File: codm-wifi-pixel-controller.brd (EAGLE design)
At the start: 59 x 25.5 mm, 48 parts, among them U1 AP62XXX-TSOT26, U2 REG710NA-5/250, U3 SN74AHCT125D, U4 ESP-WROOM-32

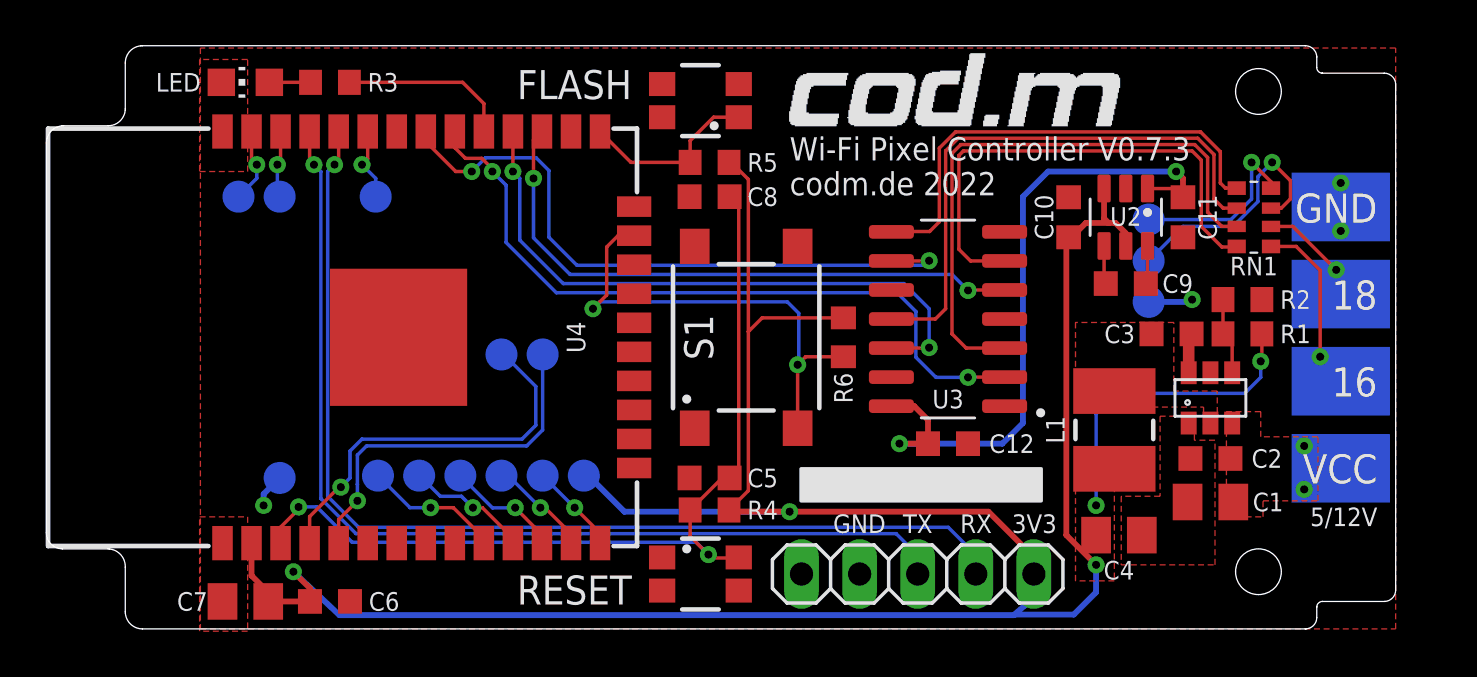
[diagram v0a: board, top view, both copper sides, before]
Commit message: added reverse polarity protection
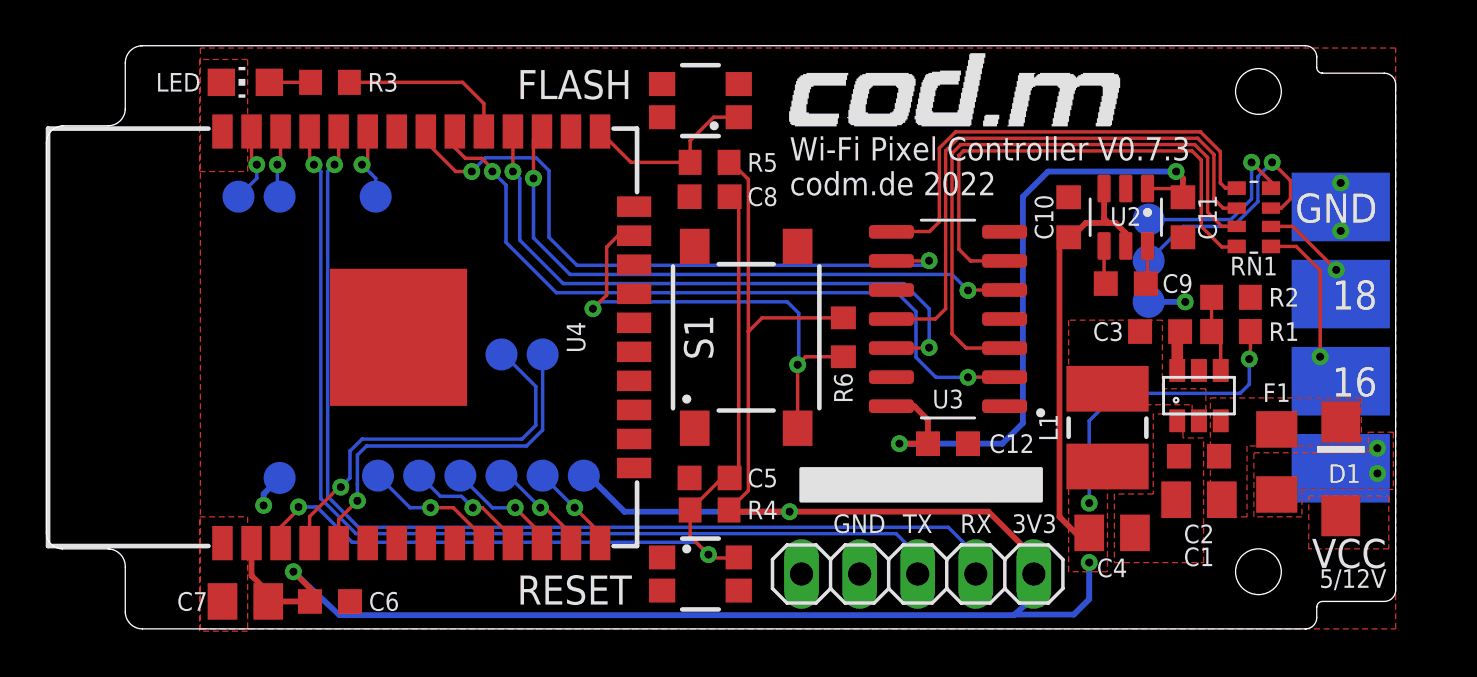
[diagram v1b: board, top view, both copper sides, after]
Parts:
- added D1: SK34A, diode:DO214AC
- added F1: 8V 500mA, adafruit:R1206
- moved C1 0.51 mm to (50.4, 5.65)
- moved C2 0.51 mm to (50.4, 7.55)
- moved C3 0.51 mm to (48.7, 13.0)
- moved R1 0.51 mm to (51.8, 13.0)
- moved R2 0.51 mm to (51.8, 14.5)
- moved U1 0.51 mm to (50.4, 10.2)
- moved L1 0.32 mm to (46.4, 8.80)
- moved C4 0.32 mm to (46.6, 4.20)
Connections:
- new net VCCF: C1.2, C2.1, D1.C, F1.2, U1.VIN
- net GND: now also D1.A
- net VCC: now also F1.1; no longer C1.2, C2.1, U1.VIN
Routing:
- net +3V3: track 124.5 -> 123.6 mm
- added copper zone on layer 1, net VCCF

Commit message: new version 0.7.4 with fixes
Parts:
- removed C8: 100n, rcl:C0603K
- added TP16: PTR1TP14R, testpad:TP14R
- JP1: device pinhead:1X05 -> codm:1X05
- U3: value SN74AHCT125D -> SN74AHCT125PWR; device SN74AHCT125D:SOIC127P600X175-14N -> SN74AHCT125PWR:SOP65P640X120-14N
- moved C11 23.8 mm to (28.1, 8.00)
- moved RN1 21.9 mm to (30.9, 18.6), turned to 180 degrees
- moved U2 19.0 mm to (31.0, 8.10), turned to 0 degrees
- moved C10 18.5 mm to (31.0, 5.60), turned to 0 degrees
- moved C9 15.0 mm to (33.9, 8.10), turned to 270 degrees
- moved S1 9.70 mm to (40.3, 12.8)
- moved C12 8.94 mm to (31.0, 11.1)
- moved TP7 8.70 mm to (48.2, 23.0)
- moved U3 8.48 mm to (31.0, 14.5)
- moved D1 7.86 mm to (49.0, 5.00)
- moved R6 7.74 mm to (40.3, 7.25), turned to 180 degrees
- moved C5 6.38 mm to (33.8, 2.40), turned to 270 degrees
- moved C4 5.00 mm to (46.6, 9.20)
- moved R4 4.33 mm to (32.3, 2.40), turned to 270 degrees
- moved L1 4.30 mm to (46.4, 13.1)
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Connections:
- net BTN: now also S1.1; no longer S1.2
- net GND: now also FLASH.4, RESET.2, S1.2, TP16.TP; no longer C8.1, FLASH.3, RESET.1, S1.1
- net RESET: no longer C8.2
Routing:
- net IO18-5VR: track 4.78 -> 29.9 mm
- net +5V: track 29.9 -> 8.36 mm, vias 2 -> 0
- net IO16-5VR: track 7.80 -> 28.2 mm
- net IO18-5V: track 25.9 -> 6.05 mm
- net IO17-5V: track 24.8 -> 5.19 mm
- net IO16-5V: track 22.0 -> 3.38 mm
- net IO19-5V: track 20.6 -> 2.62 mm
- net RESET: track 39.3 -> 26.8 mm
- net IO19-5VR: track 7.95 -> 20.1 mm
- net IO17: track 27.4 -> 16.7 mm
- net IO18: track 31.6 -> 22.0 mm
- net IO19: track 28.6 -> 19.3 mm
- net IO17-5VR: track 10.8 -> 19.3 mm
- net IO16: track 26.4 -> 18.6 mm
- net +3V3: track 123.6 -> 116.5 mm, vias 5 -> 7
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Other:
- board text added: "90060-0.7.4"
- board text added: "Wi-Fi Pixel Controller V0.7.4"
- board text added: "Wi-Fi Pixel Controller V0.7.4 codm.de 2022"
- board text added: "codm.de 2022"
- board text removed: "90060-0.7.3"
- board text removed: "Wi-Fi Pixel Controller V0.7.3 codm.de 2022"
- board text removed: "Wi-Fi Pixel Controller V0.7.3 codm.de, 2022 CC-BY-NC-SA"

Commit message: finetuning 0.7.4
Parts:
- removed R5: 10k, rcl:R0603
- added U$2: (no value), codm:WLED-INSIDE-LOGO-10MM
- F1: value 8V 500mA -> 24V 500mA
- moved U$102 9.31 mm to (36.5, 11.2)
- moved U$100 4.53 mm to (31.9, 6.60)
- moved R6 0.10 mm to (40.2, 7.25)
- moved S1 0.10 mm to (40.2, 12.8)
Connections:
- net +3V3: no longer R5.1
- net GPIO0: no longer R5.2
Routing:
- net +3V3: track 116.5 -> 97.4 mm, vias 7 -> 5
- net GPIO0: track 9.36 -> 6.92 mm
- net +5V: track 8.36 -> 6.84 mm
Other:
- board text added: "IO0"
- board text added: "IO15"

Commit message: after prototype 0.7.4 - final 0.8
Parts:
- removed C12: 100n, rcl:C0603K
- added C8: 2.2uF, rcl:C0603K
- C11: value 2.2uF -> 100n
- moved C11 4.24 mm to (31.0, 11.1), turned to 180 degrees
- moved C9 3.83 mm to (31.0, 5.60), turned to 0 degrees
- moved C10 3.76 mm to (28.1, 8.00), turned to 90 degrees
- renumbered R6 to R5
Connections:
- net +3V3: now also C9.2; no longer C10.2
- net +5V: now also C10.2; no longer C12.2
- net GND: now also C9.1; no longer C12.1
- net N$5: now also C8.1; no longer C9.1
- net N$8: now also C8.2; no longer C9.2
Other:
- board text added: "90060-0.8"
- board text added: "CC-BY-NC-SA 4.0"
- board text added: "Wi-Fi Pixel Controller V0.8"
- board text added: "Wi-Fi Pixel Controller V0.8 codm.de 2022"
- board text removed: "90060-0.7.4"
- board text removed: "Wi-Fi Pixel Controller V0.7.4"
- board text removed: "Wi-Fi Pixel Controller V0.7.4 codm.de 2022"
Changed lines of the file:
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@@
 <text x="43.95" y="3.7" size="0.8128" layer="25" font="vector" align="center">RX</text>
 <text x="46.5" y="3.7" size="0.8128" layer="25" font="vector" align="center">3V3</text>
-<text x="34.6" y="21.1" size="1.016" layer="25" font="vector" ratio="12" align="top-left">Wi-Fi Pixel Controller V0.7.4
+<text x="34.6" y="21.1" size="1.016" layer="25" font="vector" ratio="12" align="top-left">Wi-Fi Pixel Controller V0.8
 codm.de 2022</text>
-<text x="2.4" y="13.2" size="1.4224" layer="26" font="vector" rot="MR90" align="center">90060-0.7.4</text>
-<text x="58.2" y="18.4" size="1.27" layer="25" ratio="15" align="center-right">GND</text>
-<text x="58.2" y="14.6" size="1.27" layer="25" ratio="15" align="center-right">18</text>
-<text x="58.2" y="10.8" size="1.27" layer="25" ratio="15" align="center-right">16</text>
-<text x="58.2" y="7" size="1.27" layer="25" ratio="15" align="center-right">VCC</text>
-<text x="29.5" y="17.1" size="1.4224" layer="26" ratio="12" rot="MR0" align="center">Wi-Fi Pixel Controller V0.7.4</text>
+<text x="2.4" y="13.2" size="1.4224" layer="26" font="vector" rot="MR90" align="center">90060-0.8</text>
+<text x="58.2" y="18.4" size="1.27" layer="25" ratio="20" align="center-right">GND</text>
+<text x="58.2" y="14.6" size="1.27" layer="25" ratio="20" align="center-right">18</text>
+<text x="58.2" y="10.8" size="1.27" layer="25" ratio="20" align="center-right">16</text>
+<text x="58.2" y="7" size="1.27" layer="25" ratio="20" align="center-right">VCC</text>
+<text x="29.5" y="17.1" size="1.4224" layer="26" ratio="12" rot="MR0" align="center">Wi-Fi Pixel Controller V0.8</text>
 <circle x="8" y="7" radius="1" width="0" layer="29"/>
 <circle x="56" y="22" radius="1" width="0" layer="29"/>
@@
 <wire x1="3.45" y1="22.75" x2="3.4472" y2="22.6846" width="0" layer="20"/>
 <wire x1="2.7" y1="22" x2="3.4472" y2="22.6846" width="0" layer="20" curve="85.0001"/>
-<text x="29.5" y="24" size="1.27" layer="26" ratio="12" rot="MR0" align="center">CC-BY-NC-SA</text>
+<text x="29.5" y="24" size="1.27" layer="26" ratio="12" rot="MR0" align="center">CC-BY-NC-SA 4.0</text>
 <text x="29.5" y="4.1" size="1.27" layer="26" rot="MR0" align="center">codm.de 2022</text>
 <text x="18.1" y="13.1" size="0.8128" layer="26" rot="MR90" align="center-left">GND</text>
@@
 <attribute name="VALUE" x="34.6" y="19.3" size="1.27" layer="27" rot="R180" align="top-left"/>
 </element>
-<element name="C12" library="rcl" package="C0603K" package3d_urn="urn:adsk.eagle:package:23680/2" value="100n" x="31" y="11.1" smashed="yes" rot="R180">
+<element name="C11" library="rcl" package="C0603K" package3d_urn="urn:adsk.eagle:package:23680/2" value="100n" x="31" y="11.1" smashed="yes" rot="R180">
 <attribute name="NAME" x="32.6" y="11.1" size="0.8128" layer="25" align="center-left"/>
 <attribute name="POPULARITY" value="30" x="31" y="11.1" size="1.778" layer="27" rot="R180" display="off"/>
@@
 </element>
 <element name="R1" library="rcl" package="R0603" package3d_urn="urn:adsk.eagle:package:23555/3" value="69k8" x="51.8" y="17" smashed="yes" rot="R180">
-<attribute name="NAME" x="53.45" y="17" size="0.8128" layer="25" align="center-left"/>
+<attribute name="NAME" x="52.3" y="15.8" size="0.8128" layer="25" align="center-left"/>
 <attribute name="POPULARITY" value="70" x="51.8" y="17" size="1.778" layer="27" rot="R180" display="off"/>
 <attribute name="SPICEPREFIX" value="R" x="51.8" y="17" size="1.778" layer="27" rot="R180" display="off"/>
@@
 </element>
 <element name="R2" library="rcl" package="R0603" package3d_urn="urn:adsk.eagle:package:23555/3" value="22k1" x="51.8" y="18.5" smashed="yes">
-<attribute name="NAME" x="53.45" y="18.5" size="0.8128" layer="25" align="center-left"/>
+<attribute name="NAME" x="50.25" y="18.5" size="0.8128" layer="25" align="center-right"/>
 <attribute name="POPULARITY" value="70" x="51.8" y="18.5" size="1.778" layer="27" display="off"/>
 <attribute name="SPICEPREFIX" value="R" x="51.8" y="18.5" size="1.778" layer="27" display="off"/>
@@
 <attribute name="VALUE" x="28.1" y="5.1" size="1.27" layer="27"/>
 </element>
-<element name="C10" library="rcl" package="C0603K" package3d_urn="urn:adsk.eagle:package:23680/2" value="2.2uF" x="31" y="5.6" smashed="yes">
+<element name="C9" library="rcl" package="C0603K" package3d_urn="urn:adsk.eagle:package:23680/2" value="2.2uF" x="31" y="5.6" smashed="yes">
 <attribute name="NAME" x="29.3" y="5.6" size="0.8128" layer="25" align="center-right"/>
 <attribute name="POPULARITY" value="30" x="31" y="5.6" size="1.778" layer="27" display="off"/>
@@
 <attribute name="VALUE" x="30.2" y="3.95" size="1.016" layer="27"/>
 </element>
-<element name="C11" library="rcl" package="C0603K" package3d_urn="urn:adsk.eagle:package:23680/2" value="2.2uF" x="28.1" y="8" smashed="yes" rot="R90">
+<element name="C10" library="rcl" package="C0603K" package3d_urn="urn:adsk.eagle:package:23680/2" value="2.2uF" x="28.1" y="8" smashed="yes" rot="R90">
 <attribute name="NAME" x="28.1" y="9.627" size="0.8128" layer="25" align="bottom-center"/>
 <attribute name="POPULARITY" value="30" x="33.1" y="3" size="1.778" layer="27" rot="R90" display="off"/>
@@
 <attribute name="VALUE" x="29.75" y="7.2" size="1.016" layer="27" rot="R90"/>
 </element>
-<element name="C9" library="rcl" package="C0603K" package3d_urn="urn:adsk.eagle:package:23680/2" value="2.2uF" x="33.9" y="8.1" smashed="yes" rot="R270">
+<element name="C8" library="rcl" package="C0603K" package3d_urn="urn:adsk.eagle:package:23680/2" value="2.2uF" x="33.9" y="8.1" smashed="yes" rot="R270">
 <attribute name="NAME" x="33.9" y="6.473" size="0.8128" layer="25" align="top-center"/>
 <attribute name="POPULARITY" value="30" x="28.9" y="8.1" size="1.778" layer="27" rot="R270" display="off"/>
@@
 <attribute name="VALUE" value="430182070816" x="45.1834" y="9.568" size="1.27" layer="27" rot="R90"/>
 </element>
-<element name="R6" library="rcl" package="R0603" package3d_urn="urn:adsk.eagle:package:23555/3" value="10k" x="40.2" y="7.25" smashed="yes" rot="R180">
+<element name="R5" library="rcl" package="R0603" package3d_urn="urn:adsk.eagle:package:23555/3" value="10k" x="40.2" y="7.25" smashed="yes" rot="R180">
 <attribute name="NAME" x="38.65" y="7.25" size="0.8128" layer="25" rot="R180" align="center-left"/>
 <attribute name="POPULARITY" value="70" x="40.2" y="7.25" size="1.778" layer="27" rot="R180" display="off"/>
@@
 <contactref element="U$101" pad="P$1"/>
 <contactref element="U3" pad="7"/>
-<contactref element="C12" pad="1"/>
+<contactref element="C11" pad="1"/>
 <via x="56.6" y="19.5" extent="1-16" drill="0.35" shape="octagon"/>
 <via x="56.6" y="17.4" extent="1-16" drill="0.35" shape="octagon"/>
@@
 <contactref element="C4" pad="2"/>
 <contactref element="U2" pad="2"/>
+<contactref element="C9" pad="1"/>
 <contactref element="C10" pad="1"/>
-<contactref element="C11" pad="1"/>
 <contactref element="U1" pad="GND"/>
 <contactref element="C2" pad="2"/>
@@
 <signal name="+5V">
 <contactref element="U3" pad="14"/>
-<contactref element="C12" pad="2"/>
+<contactref element="C11" pad="2"/>
 <contactref element="U2" pad="1"/>
-<contactref element="C11" pad="2"/>
+<contactref element="C10" pad="2"/>
 <wire x1="29.745" y1="9.05" x2="29.715" y2="9.02" width="0.1524" layer="1"/>
 <wire x1="29.715" y1="9.02" x2="28.146603125" y2="9.02" width="0.254" layer="1"/>
@@
 <contactref element="C4" pad="1"/>
 <contactref element="U2" pad="3"/>
-<contactref element="C10" pad="2"/>
+<contactref element="C9" pad="2"/>
 <contactref element="U2" pad="5"/>
 <polygon width="0.254" layer="1" thermals="no">
@@
 <wire x1="31.15" y1="6.45" x2="32" y2="5.6" width="0.254" layer="1"/>
 <wire x1="32" y1="5.6" x2="32.4" y2="5.2" width="0.254" layer="1"/>
-<contactref element="R6" pad="1"/>
+<contactref element="R5" pad="1"/>
 <wire x1="45.7" y1="0.8" x2="35.2" y2="0.8" width="0.254" layer="16"/>
 <wire x1="35.2" y1="0.8" x2="12.696890625" y2="0.8" width="0.254" layer="16"/>
@@
 <signal name="N$5">
 <contactref element="U2" pad="6"/>
-<contactref element="C9" pad="1"/>
+<contactref element="C8" pad="1"/>
 <wire x1="32.255" y1="9.05" x2="33.825" y2="9.05" width="0.1524" layer="1"/>
 <wire x1="33.825" y1="9.05" x2="33.9" y2="8.975" width="0.1524" layer="1"/>
 </signal>
 <signal name="N$8">
-<contactref element="C9" pad="2"/>
+<contactref element="C8" pad="2"/>
 <contactref element="U2" pad="4"/>
 <wire x1="32.255" y1="7.15" x2="33.825" y2="7.15" width="0.1524" layer="1"/>
@@
 </signal>
 <signal name="BTN">
-<contactref element="R6" pad="2"/>
+<contactref element="R5" pad="2"/>
 <contactref element="U4" pad="23"/>
 <contactref element="S1" pad="1"/>

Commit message: final V0.8, edited readme
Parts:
- LED: value 150080RS75000 -> 150080GS75000
